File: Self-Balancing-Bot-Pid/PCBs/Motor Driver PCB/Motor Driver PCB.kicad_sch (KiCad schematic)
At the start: 23 parts, among them IC1 AS5600-ASOT, J1 Conn_01x08_Pin, U1 A4988SETTR-T

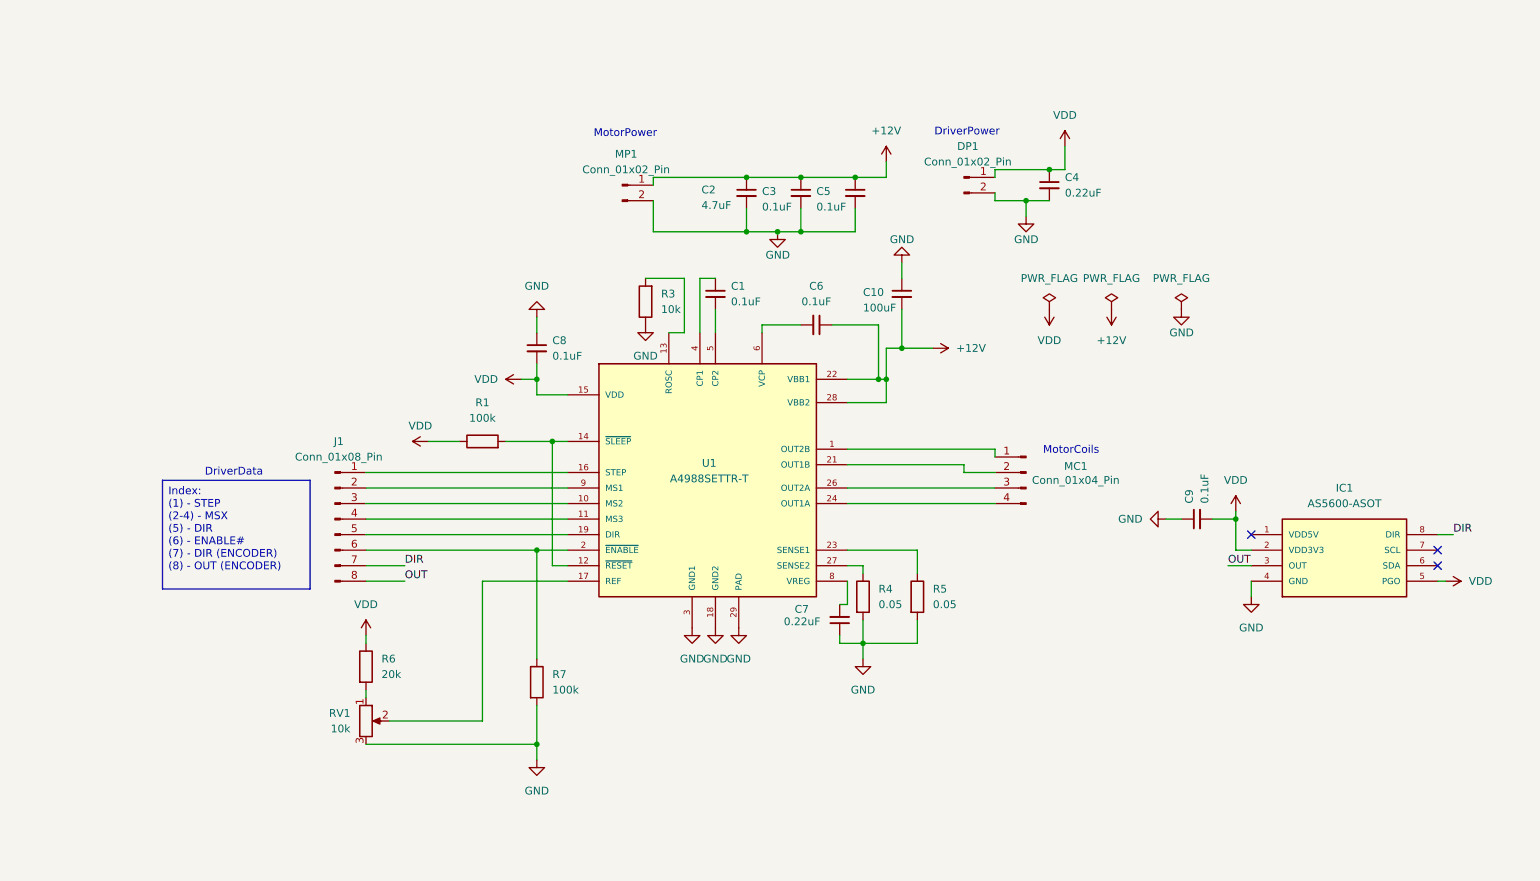
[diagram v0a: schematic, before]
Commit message: Made sure PWR flags are all pointed up and GND flags are pointed down
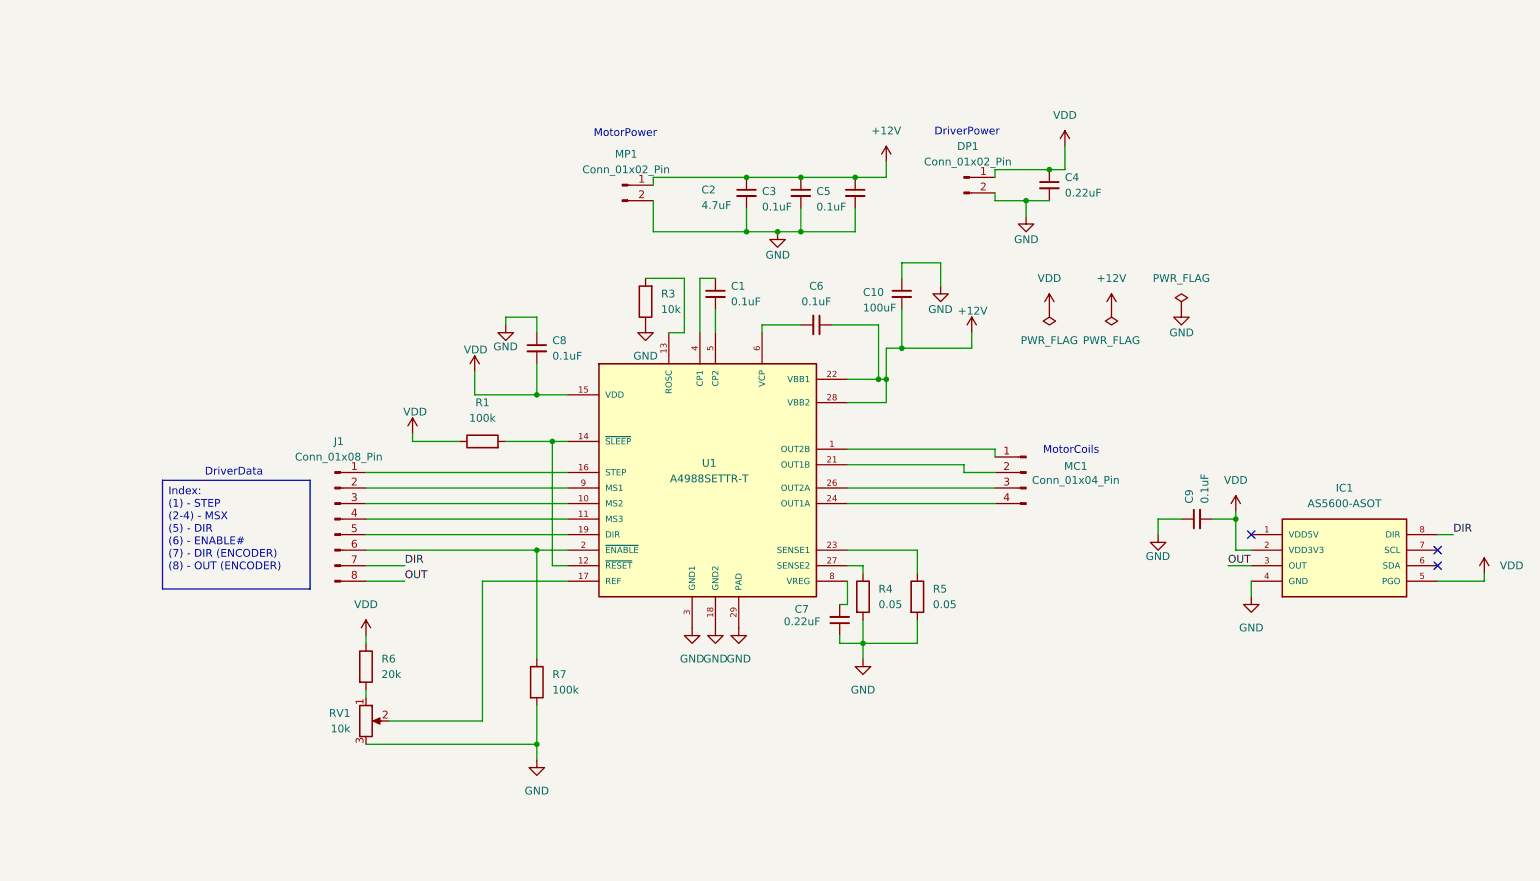
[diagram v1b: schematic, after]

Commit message: Updated schematic: changed R6 value to 33k, used more net labels for a cleaner schematic, switched the bulk capacitor to a SMD Electrolytic Can footprint. Ensured the sense resistors used are rated for 1W.
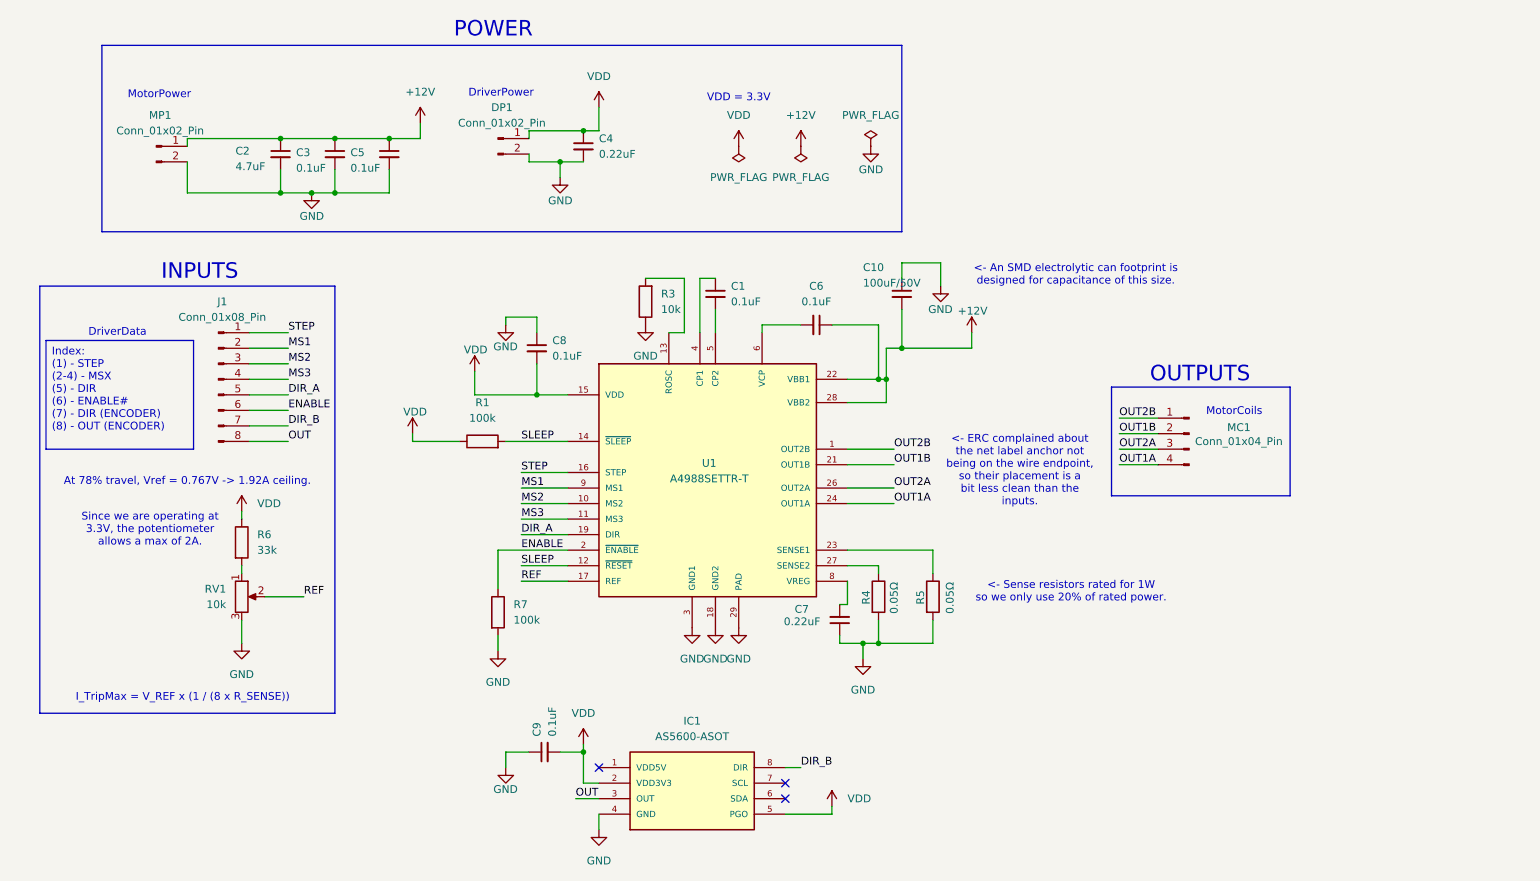
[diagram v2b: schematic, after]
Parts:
- C10: value 100uF -> 100uF/50V; footprint Capacitor_SMD:C_0603_1608Metric -> Capacitor_SMD:CP_Elec_8x10.5; MPN (none) -> UWT1H101MNL1GS
- R4, R5: value 0.05 -> 0.05Ω; footprint Resistor_SMD:R_0603_1608Metric -> Resistor_SMD:R_2512_6332Metric; MPN (none) -> WSL2512R0500FEA; Wattage (none) -> 1W
- R6: value 20k -> 33k
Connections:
- net OUT2B: now reaches MC1.1 (Pin_1), U1.1 (OUT2B)
- net OUT1B: now reaches MC1.2 (Pin_2), U1.21 (OUT1B)
- net OUT2A: now reaches MC1.3 (Pin_3), U1.26 (OUT2A)
- net OUT1A: now reaches MC1.4 (Pin_4), U1.24 (OUT1A)
- net STEP: now reaches J1.1 (Pin_1), U1.16 (STEP)
- net MS1: now reaches J1.2 (Pin_2), U1.9 (MS1)
- net MS2: now reaches J1.3 (Pin_3), U1.10 (MS2)
- net MS3: now reaches J1.4 (Pin_4), U1.11 (MS3)
- net DIR_A: now reaches J1.5 (Pin_5), U1.19 (DIR)
- net ENABLE: now reaches J1.6 (Pin_6), R7.1, U1.2 (~{ENABLE})
- net SLEEP: now reaches R1.2, U1.12 (~{RESET}), U1.14 (~{SLEEP})
- net REF: now reaches RV1.2, U1.17 (REF)
- net DIR renamed DIR_B
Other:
- note added: "<- An SMD electrolytic can footprint is designed for capacitance of this size."
- note added: "<- ERC complained about the net label anchor not being on the wire endpoint, so their placement is a bit less clean than the inputs."
- note added: "<- Sense resistors rated for 1W so we only use 20% of rated power."
- note added: "At 78% travel, Vref = 0.767V -> 1.92A ceiling."
- note added: "INPUTS"
- note added: "I_TripMax = V_REF x (1 / (8 x R_SENSE))"
- note added: "OUTPUTS"
- note added: "POWER"
- note added: "Since we are operating at 3.3V, the potentiometer allows a max of 2A."
- note added: "VDD = 3.3V"
- moved on the sheet: C2, C3, C4, C5, C9, DP1, IC1, J1, MC1, MP1, R4, R5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

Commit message: Started rerouting and placing components and terminals in more elegant places. Expanded the copper pour and brought the as5600 IC to the front side.
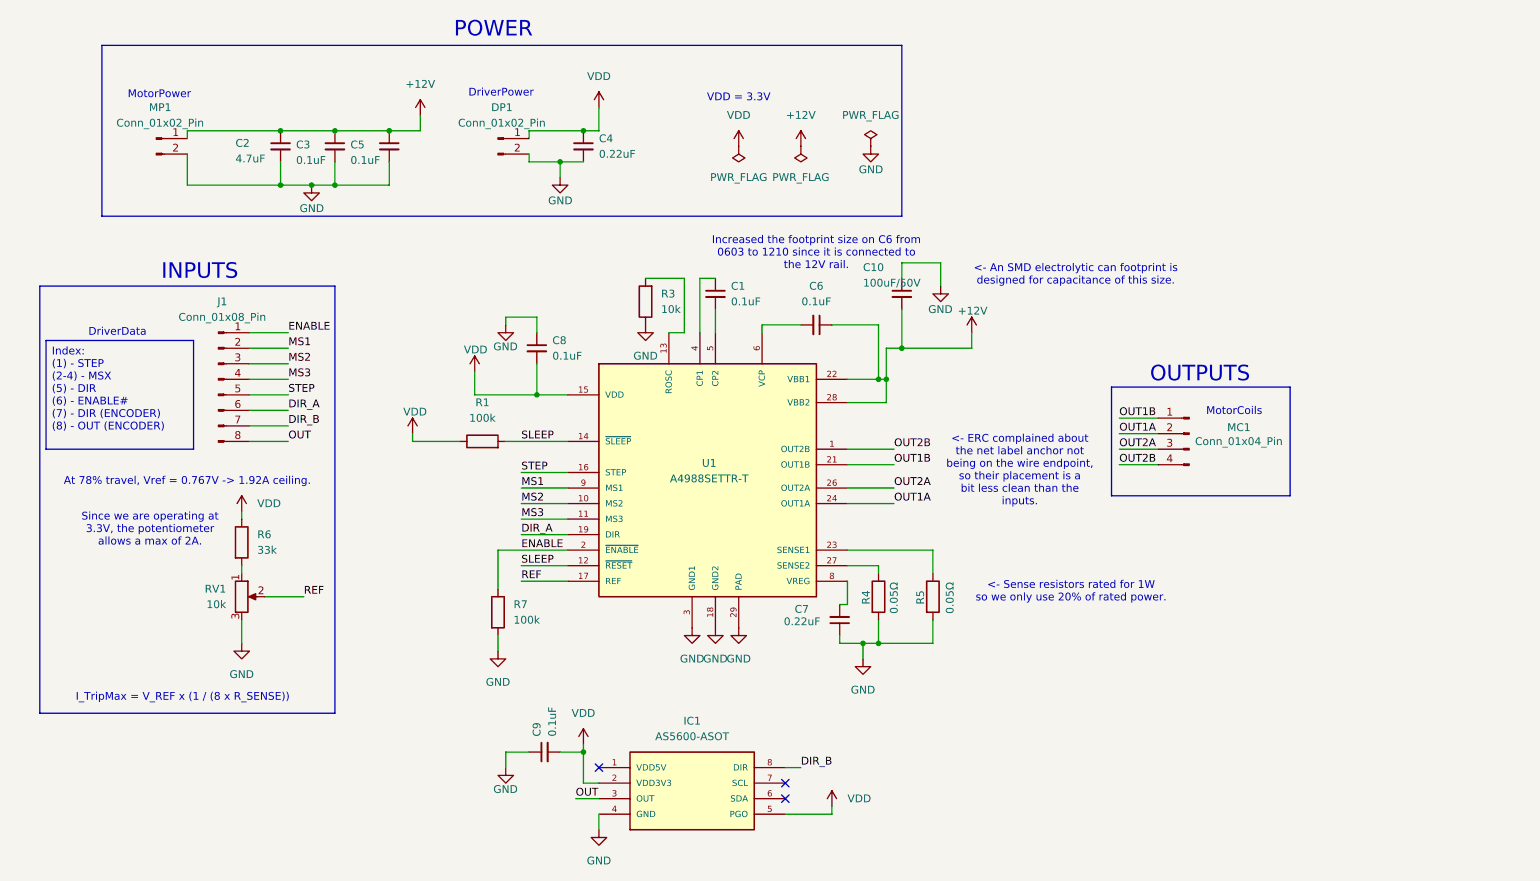
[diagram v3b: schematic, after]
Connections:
- net DIR_A: now also J1.6 (Pin_6); no longer J1.5 (Pin_5)
- net ENABLE: now also J1.1 (Pin_1); no longer J1.6 (Pin_6)
- net OUT1A: now also MC1.2 (Pin_2); no longer MC1.4 (Pin_4)
- net OUT1B: now also MC1.1 (Pin_1); no longer MC1.2 (Pin_2)
- net OUT2B: now also MC1.4 (Pin_4); no longer MC1.1 (Pin_1)
- net STEP: now also J1.5 (Pin_5); no longer J1.1 (Pin_1)
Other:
- note added: "Increased the footprint size on C6 from 0603 to 1210 since it is connected to the 12V rail."
- moved on the sheet: C2, C3, C5, MP1
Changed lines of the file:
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@@
 		)
 	)
+	(text "Increased the footprint size on C6 from \n0603 to 1210 since it is connected to \nthe 12V rail."
+		(exclude_from_sim no)
+		(at 147.32 59.436 0)
+		(effects
+			(font
+				(size 1.27 1.27)
+			)
+		)
+	)
 	(text "Since we are operating at\n3.3V, the potentiometer \nallows a max of 2A."
 		(exclude_from_sim no)
@@
 		(exclude_from_sim no)
 		(at 30.48 25.4 0)
-		(size 130.81 30.48)
+		(size 130.81 27.94)
 		(margins 0.9525 0.9525 0.9525 0.9525)
 		(stroke
@@
 	)
 	(junction
-		(at 64.77 49.53)
+		(at 64.77 48.26)
 		(diameter 0)
 		(color 0 0 0 0)
 	)
 	(junction
-		(at 59.69 40.64)
+		(at 59.69 39.37)
 		(diameter 0)
 		(color 0 0 0 0)
@@
 	)
 	(junction
-		(at 77.47 40.64)
+		(at 77.47 39.37)
 		(diameter 0)
 		(color 0 0 0 0)
 	)
 	(junction
-		(at 68.58 40.64)
+		(at 68.58 39.37)
 		(diameter 0)
 		(color 0 0 0 0)
@@
 	)
 	(junction
-		(at 59.69 49.53)
+		(at 59.69 48.26)
 		(diameter 0)
 		(color 0 0 0 0)
 	)
 	(junction
-		(at 68.58 49.53)
+		(at 68.58 48.26)
 		(diameter 0)
 		(color 0 0 0 0)
@@
 	(wire
 		(pts
-			(xy 59.69 40.64) (xy 44.45 40.64)
+			(xy 59.69 39.37) (xy 44.45 39.37)
 		)
 		(stroke
@@
 	(wire
 		(pts
-			(xy 59.69 45.72) (xy 59.69 49.53)
+			(xy 59.69 44.45) (xy 59.69 48.26)
 		)
 		(stroke
@@
 	(wire
 		(pts
-			(xy 64.77 49.53) (xy 68.58 49.53)
+			(xy 64.77 48.26) (xy 68.58 48.26)
 		)
 		(stroke
@@
 	(wire
 		(pts
-			(xy 59.69 49.53) (xy 44.45 49.53)
+			(xy 59.69 48.26) (xy 44.45 48.26)
 		)
 		(stroke
@@
 	(wire
 		(pts
-			(xy 44.45 40.64) (xy 44.45 41.91)
+			(xy 44.45 39.37) (xy 44.45 40.64)
 		)
 		(stroke
@@
 	(wire
 		(pts
-			(xy 68.58 40.64) (xy 77.47 40.64)
+			(xy 68.58 39.37) (xy 77.47 39.37)
 		)
 		(stroke
@@
 	(wire
 		(pts
-			(xy 77.47 45.72) (xy 77.47 49.53)
+			(xy 77.47 44.45) (xy 77.47 48.26)
 		)
 		(stroke
@@
 	(wire
 		(pts
-			(xy 68.58 45.72) (xy 68.58 49.53)
+			(xy 68.58 44.45) (xy 68.58 48.26)
 		)
 		(stroke
@@
 	(wire
 		(pts
-			(xy 82.55 38.1) (xy 82.55 40.64)
+			(xy 82.55 36.83) (xy 82.55 39.37)
 		)
 		(stroke
@@
 	(wire
 		(pts
-			(xy 59.69 40.64) (xy 68.58 40.64)
+			(xy 59.69 39.37) (xy 68.58 39.37)
 		)
 		(stroke
@@
 	(wire
 		(pts
-			(xy 59.69 49.53) (xy 64.77 49.53)
+			(xy 59.69 48.26) (xy 64.77 48.26)
 		)
 		(stroke
@@
 	(wire
 		(pts
-			(xy 44.45 49.53) (xy 44.45 44.45)
+			(xy 44.45 48.26) (xy 44.45 43.18)
 		)
 		(stroke
@@
 	(wire
 		(pts
-			(xy 77.47 40.64) (xy 82.55 40.64)
+			(xy 77.47 39.37) (xy 82.55 39.37)
 		)
 		(stroke
@@
 	(wire
 		(pts
-			(xy 68.58 49.53) (xy 77.47 49.53)
+			(xy 68.58 48.26) (xy 77.47 48.26)
 		)
 		(stroke
@@
 	)
 	(label "STEP"
-		(at 60.96 72.39 0)
+		(at 60.96 82.55 0)
 		(effects
 			(font
@@
 	)
 	(label "DIR_A"
-		(at 60.96 82.55 0)
+		(at 60.96 85.09 0)
 		(effects
 			(font
@@
 	)
 	(label "ENABLE"
-		(at 60.96 85.09 0)
+		(at 60.96 72.39 0)
 		(effects
 			(font
@@
 	)
 	(label "OUT1B"
-		(at 196.85 88.9 0)
+		(at 196.85 86.36 0)
 		(effects
 			(font
@@
 	)
 	(label "OUT1A"
-		(at 196.85 93.98 0)
+		(at 196.85 88.9 0)
 		(effects
 			(font
@@
 	)
 	(label "OUT2B"
-		(at 196.85 86.36 0)
+		(at 196.85 93.98 0)
 		(effects
 			(font
@@
 	(symbol
 		(lib_id "power:+12V")
-		(at 82.55 38.1 0)
+		(at 82.55 36.83 0)
 		(unit 1)
 		(exclude_from_sim no)
@@
 		(fields_autoplaced yes)
 		(property "Reference" "#PWR04"
-			(at 82.55 41.91 0)
+			(at 82.55 40.64 0)
 			(effects
 				(font
@@
 		)
 		(property "Value" "+12V"
-			(at 82.55 33.02 0)
+			(at 82.55 31.75 0)
 			(effects
 				(font
@@
 		)
 		(property "Footprint" ""
-			(at 82.55 38.1 0)
+			(at 82.55 36.83 0)
 			(effects
 				(font
@@
 		)
 		(property "Datasheet" ""
-			(at 82.55 38.1 0)
+			(at 82.55 36.83 0)
 			(effects
 				(font
@@
 		)
 		(property "Description" "Power symbol creates a global label with name \"+12V\""
-			(at 82.55 38.1 0)
+			(at 82.55 36.83 0)
 			(effects
 				(font
@@
 	(symbol
 		(lib_id "Connector:Conn_01x02_Pin")
-		(at 39.37 41.91 0)
+		(at 39.37 40.64 0)
 		(unit 1)
 		(exclude_from_sim no)
@@
 		(fields_autoplaced yes)
 		(property "Reference" "MP1"
-			(at 40.005 36.83 0)
+			(at 40.005 35.56 0)
 			(effects
 				(font
@@
 		)
 		(property "Value" "Conn_01x02_Pin"
-			(at 40.005 39.37 0)
+			(at 40.005 38.1 0)
 			(effects
 				(font
@@
 		)
 		(property "Footprint" "Connector_JST:JST_PH_B2B-PH-K_1x02_P2.00mm_Vertical"
-			(at 39.37 41.91 0)
+			(at 39.37 40.64 0)
 			(effects
 				(font
@@
 		)
 		(property "Datasheet" "~"
-			(at 39.37 41.91 0)
+			(at 39.37 40.64 0)
 			(effects
 				(font
@@
 		)
 		(property "Description" "Generic connector, single row, 01x02, script generated"
-			(at 39.37 41.91 0)
+			(at 39.37 40.64 0)
 			(effects
 				(font
@@
 	(symbol
 		(lib_id "Device:C_Small")
-		(at 59.69 43.18 0)
+		(at 59.69 41.91 0)
 		(unit 1)
 		(exclude_from_sim no)
@@
 		(dnp no)
 		(property "Reference" "C2"
-			(at 52.324 42.672 0)
+			(at 52.324 41.402 0)
 			(effects
 				(font
@@
 		)
 		(property "Value" "4.7uF"
-			(at 52.324 45.212 0)
+			(at 52.324 43.942 0)
 			(effects
 				(font
@@
 		)
 		(property "Footprint" "Capacitor_SMD:C_0603_1608Metric"
-			(at 59.69 43.18 0)
+			(at 59.69 41.91 0)
 			(effects
 				(font
@@
 		)
 		(property "Datasheet" "~"
-			(at 59.69 43.18 0)
+			(at 59.69 41.91 0)
 			(effects
 				(font
@@
 		)
 		(property "Description" "Unpolarized capacitor, small symbol"
-			(at 59.69 43.18 0)
+			(at 59.69 41.91 0)
 			(effects
 				(font
@@
 	(symbol
 		(lib_id "power:GND")
-		(at 64.77 49.53 0)
+		(at 64.77 48.26 0)
 		(unit 1)
 		(exclude_from_sim no)
@@
 		(dnp no)
 		(property "Reference" "#PWR05"
-			(at 64.77 55.88 0)
+			(at 64.77 54.61 0)
 			(effects
 				(font
@@
 		)
 		(property "Value" "GND"
-			(at 66.802 53.34 0)
+			(at 66.802 52.07 0)
 			(effects
 				(font
@@
 		)
 		(property "Footprint" ""
-			(at 64.77 49.53 0)
+			(at 64.77 48.26 0)
 			(effects
 				(font
@@
 		)
 		(property "Datasheet" ""
-			(at 64.77 49.53 0)
+			(at 64.77 48.26 0)
 			(effects
 				(font
@@
 		)
 		(property "Description" "Power symbol creates a global label with name \"GND\" , ground"
-			(at 64.77 49.53 0)
+			(at 64.77 48.26 0)
 			(effects
 				(font
@@
 	(symbol
 		(lib_id "Device:C_Small")
-		(at 77.47 43.18 0)
+		(at 77.47 41.91 0)
 		(unit 1)
 		(exclude_from_sim no)
@@
 		(dnp no)
 		(property "Reference" "C5"
-			(at 71.12 42.926 0)
+			(at 71.12 41.656 0)
 			(effects
 				(font
@@
 		)
 		(property "Value" "0.1uF"
-			(at 71.12 45.466 0)
+			(at 71.12 44.196 0)
 			(effects
 				(font
@@
 		)
 		(property "Footprint" "Capacitor_SMD:C_0603_1608Metric"
-			(at 77.47 43.18 0)
+			(at 77.47 41.91 0)
 			(effects
 				(font
@@
 		)
 		(property "Datasheet" "~"
-			(at 77.47 43.18 0)
+			(at 77.47 41.91 0)
 			(effects
 				(font
@@
 		)
 		(property "Description" "Unpolarized capacitor, small symbol"
-			(at 77.47 43.18 0)
+			(at 77.47 41.91 0)
 			(effects
 				(font
@@
 	(symbol
 		(lib_id "Device:C_Small")
-		(at 68.58 43.18 0)
+		(at 68.58 41.91 0)
 		(unit 1)
 		(exclude_from_sim no)
@@
 		(dnp no)
 		(property "Reference" "C3"
-			(at 62.23 42.926 0)
+			(at 62.23 41.656 0)
 			(effects
 				(font
@@
 		)
 		(property "Value" "0.1uF"
-			(at 62.23 45.466 0)
+			(at 62.23 44.196 0)
 			(effects
 				(font
@@
 		)
 		(property "Footprint" "Capacitor_SMD:C_0603_1608Metric"
-			(at 68.58 43.18 0)
+			(at 68.58 41.91 0)
 			(effects
 				(font
@@
 		)
 		(property "Datasheet" "~"
-			(at 68.58 43.18 0)
+			(at 68.58 41.91 0)
 			(effects
 				(font
@@
 		)
 		(property "Description" "Unpolarized capacitor, small symbol"
-			(at 68.58 43.18 0)
+			(at 68.58 41.91 0)
 			(effects
 				(font

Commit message: Increased size of sense traces as they were too skinny
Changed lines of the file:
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@@
 		)
 	)
-	(text_box "Index:\n(1) - STEP\n(2-4) - MSX\n(5) - DIR\n(6) - ENABLE#\n(7) - DIR (ENCODER)\n(8) - OUT (ENCODER)"
+	(text_box "Index:\n(1) - ENABLE\n(2-4) - MSX\n(5) - STEP\n(6) - DIR (DRIVER)\n(7) - DIR (ENCODER)\n(8) - OUT (ENCODER)"
 		(exclude_from_sim no)
 		(at 21.336 73.66 0)
